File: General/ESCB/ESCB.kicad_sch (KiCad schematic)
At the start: 3 parts, among them J1 Power_Signal, J2 Motor, U1 BESC

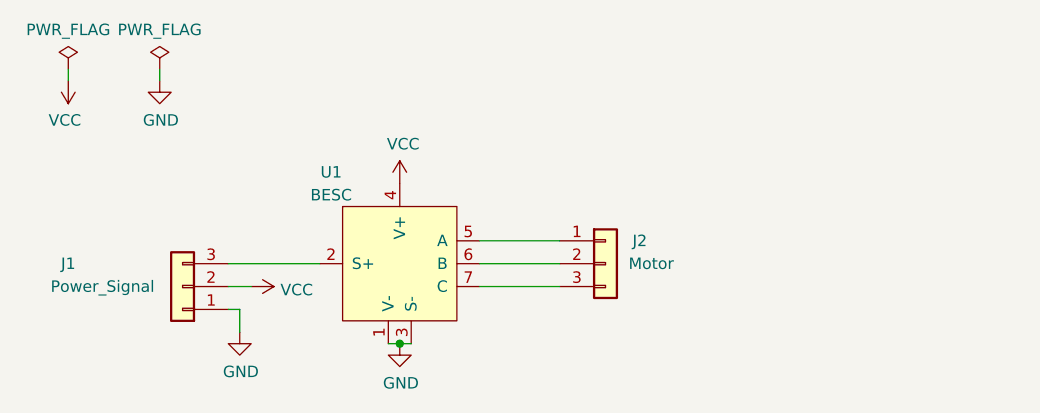
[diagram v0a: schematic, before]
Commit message: updated layout
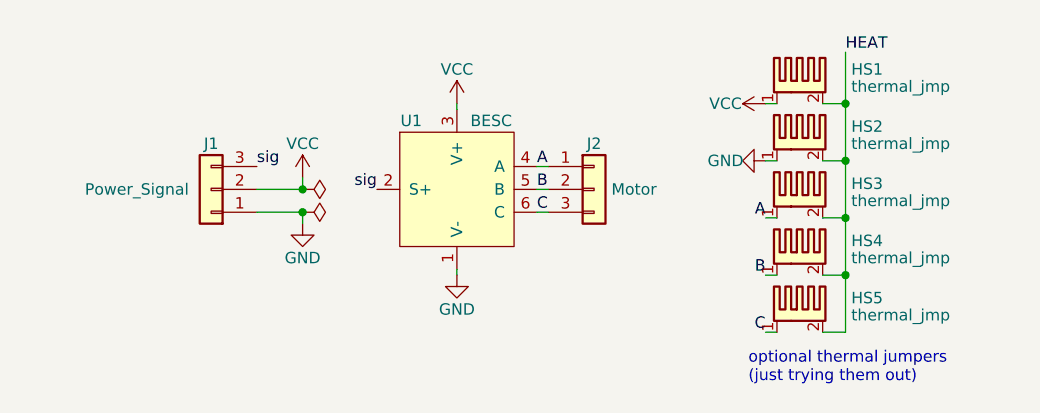
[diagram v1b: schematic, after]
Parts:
- added HS1, HS2, HS3, HS4, HS5: thermal_jmp, Resistor_SMD:R_0805_2012Metric, symbol Mechanical:Heatsink_Pad_2Pin
- J1, J2: footprint extraparts:Samtec_mPOWER_UMPS_3pin -> extraparts:Samtec_mPOWER_UMPT_3pin
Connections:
- net GND: now also HS2.1; no longer U1.3 (S-)
- net VCC: now also U1.3 (V+), HS1.1; no longer U1.4 (V+)
- net sig: now reaches J1.3 (Pin_3), U1.2 (S+)
- net A: now reaches J2.1 (Pin_1)
- net A: now also U1.4 (A), HS3.1; no longer U1.5 (A)
- net B: now reaches J2.2 (Pin_2)
- net B: now also U1.5 (B), HS4.1; no longer U1.6 (B)
- net C: now reaches J2.3 (Pin_3)
- net C: now also U1.6 (C), HS5.1; no longer U1.7 (C)
- new net HEAT: HS1.2, HS2.2, HS3.2, HS4.2, HS5.2
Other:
- note added: "optional thermal jumpers (just trying them out)"
- moved on the sheet: J1, J2
